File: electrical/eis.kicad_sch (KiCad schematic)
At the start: 51 parts

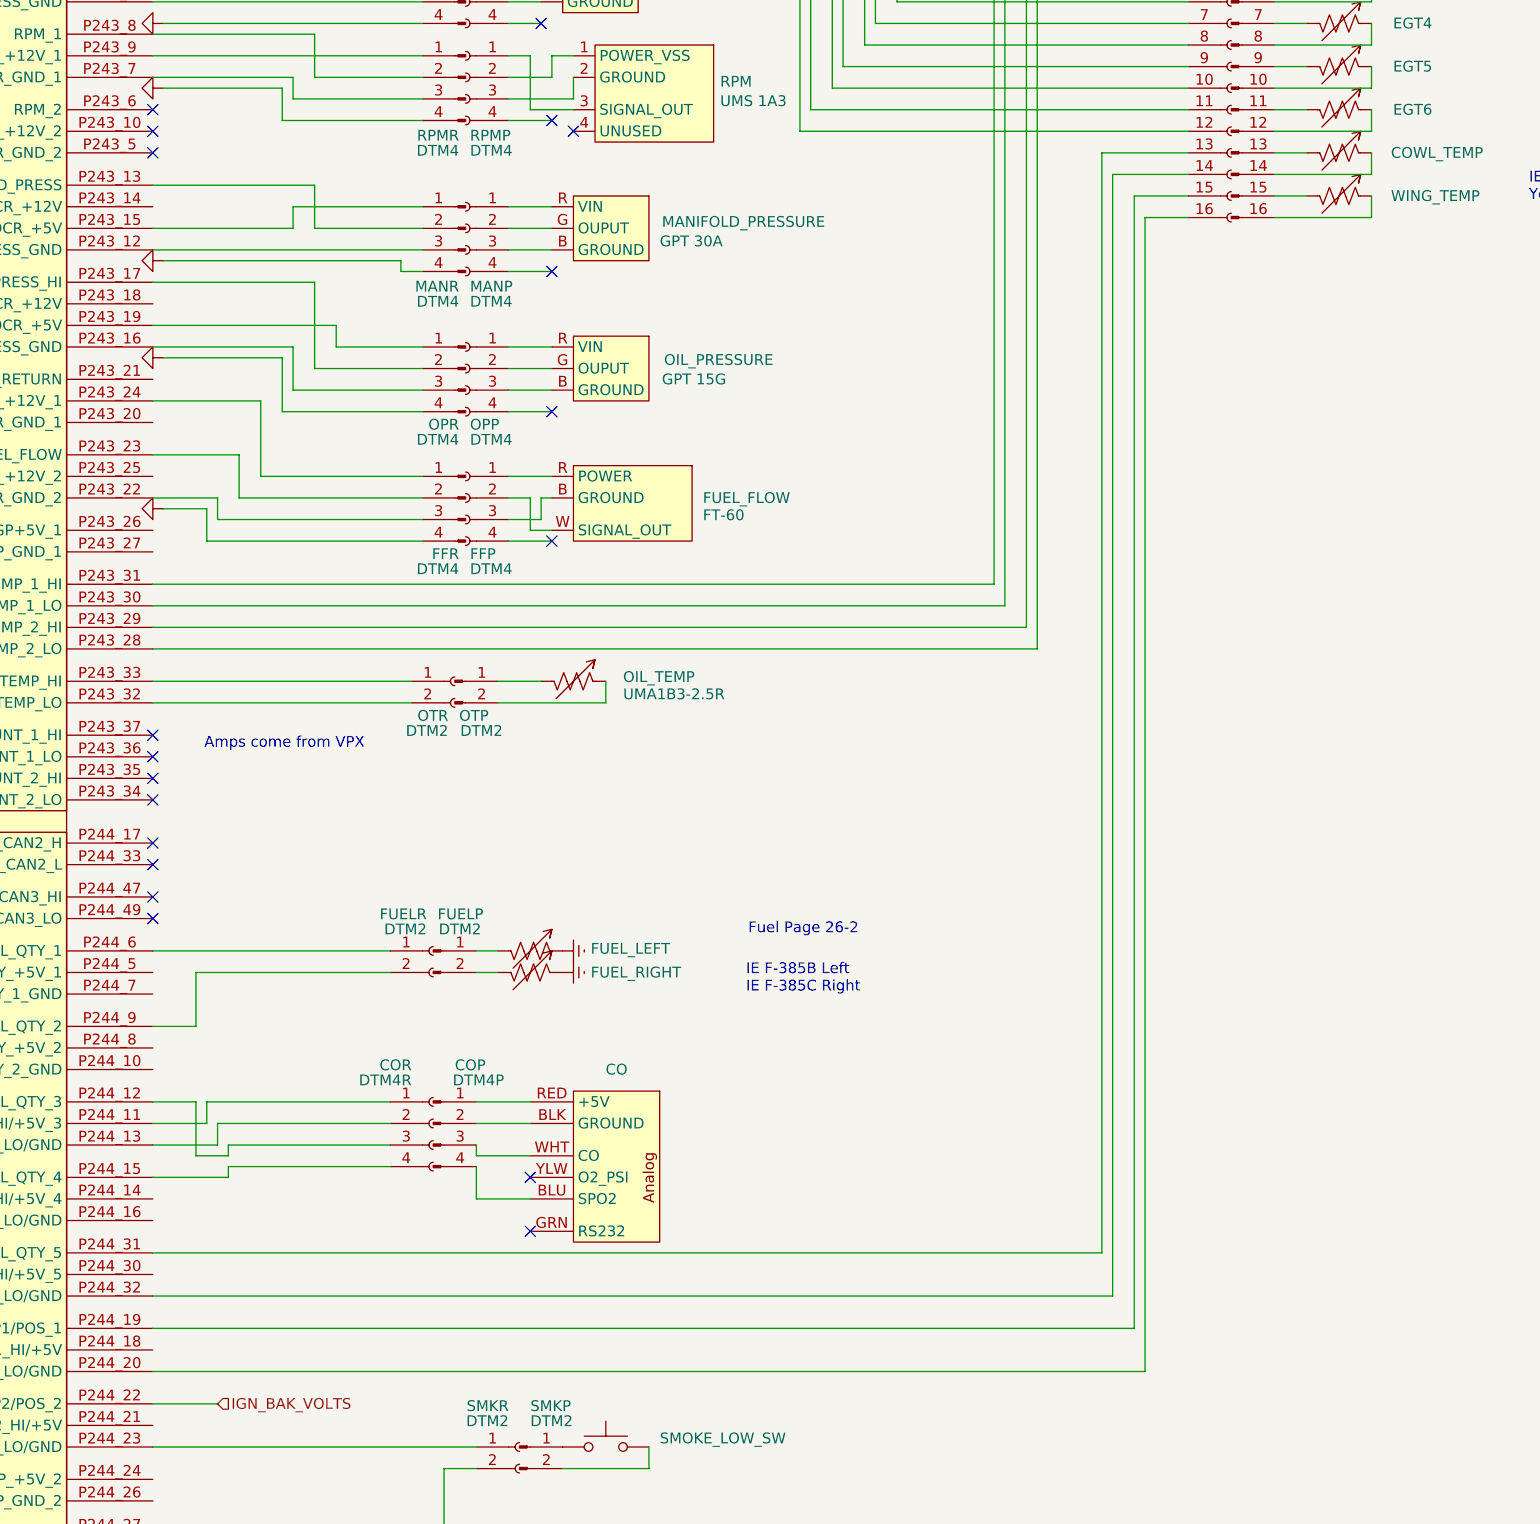
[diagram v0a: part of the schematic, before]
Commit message: Removed air temps from GP inputs as not compatible
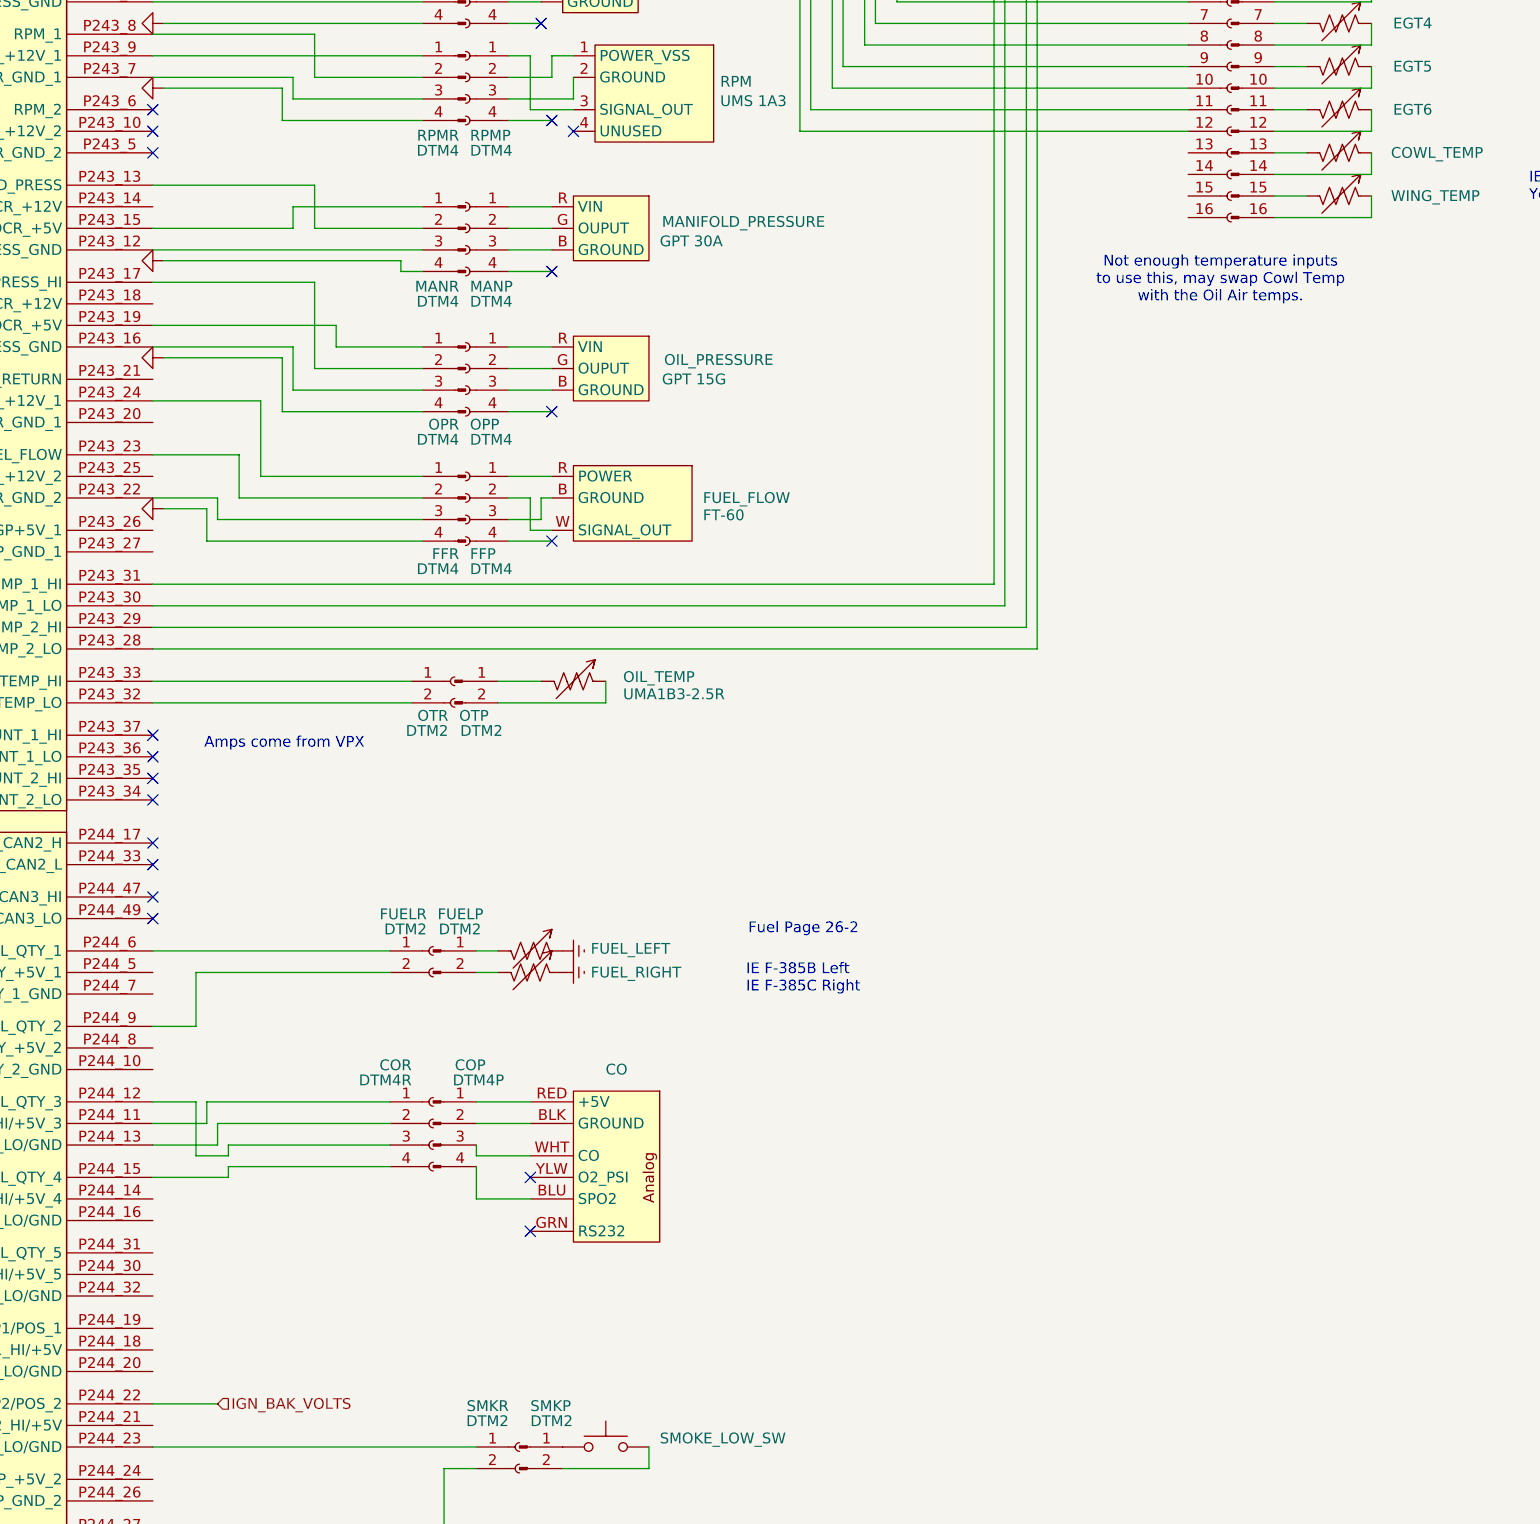
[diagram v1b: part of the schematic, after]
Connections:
- net at EGTS.13 (Pin_13): no longer GEA24.P244_31 (POS_5/GP_5/FUEL_QTY_5)
- net at EGTS.14 (Pin_14): no longer GEA24.P244_32 (POS_5_LO/GND)
- net at EGTS.15 (Pin_15): no longer GEA24.P244_19 (GP1/POS_1)
- net at EGTS.16 (Pin_16): no longer GEA24.P244_20 (GP1_LO/GND)
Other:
- note added: "Not enough temperature inputs to use this, may swap Cowl Temp with the Oil Air temps."
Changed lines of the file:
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@@
 	(title_block
 		(title "EIS")
-		(date "2025-10-22")
-		(rev "1.1.18")
+		(date "2025-10-23")
+		(rev "1.1.19")
 		(company "N78HR")
 	)
@@
 		)
 	)
+	(text "Not enough temperature inputs\nto use this, may swap Cowl Temp\nwith the Oil Air temps."
+		(exclude_from_sim no)
+		(at 193.04 152.146 0)
+		(effects
+			(font
+				(size 1.27 1.27)
+			)
+		)
+	)
 	(text "IE Probes\nYellow/Red (yellow +)"
 		(exclude_from_sim no)
@@
 	(wire
 		(pts
-			(xy 67.31 280.67) (xy 184.15 280.67)
-		)
-		(stroke
-			(width 0)
-			(type default)
-		)
-	)
-	(wire
-		(pts
 			(xy 116.84 132.08) (xy 111.76 132.08)
 		)
@@
 	(wire
 		(pts
-			(xy 182.88 275.59) (xy 182.88 142.24)
-		)
-		(stroke
-			(width 0)
-			(type default)
-		)
-	)
-	(wire
-		(pts
-			(xy 67.31 275.59) (xy 182.88 275.59)
-		)
-		(stroke
-			(width 0)
-			(type default)
-		)
-	)
-	(wire
-		(pts
 			(xy 74.93 251.46) (xy 95.25 251.46)
 		)
@@
 	(wire
 		(pts
-			(xy 180.34 139.7) (xy 180.34 271.78)
-		)
-		(stroke
-			(width 0)
-			(type default)
-		)
-	)
-	(wire
-		(pts
 			(xy 67.31 104.14) (xy 144.78 104.14)
 		)
@@
 	(wire
 		(pts
-			(xy 182.88 142.24) (xy 189.23 142.24)
-		)
-		(stroke
-			(width 0)
-			(type default)
-		)
-	)
-	(wire
-		(pts
 			(xy 67.31 187.96) (xy 166.37 187.96)
 		)
@@
 	(wire
 		(pts
-			(xy 67.31 266.7) (xy 179.07 266.7)
-		)
-		(stroke
-			(width 0)
-			(type default)
-		)
-	)
-	(wire
-		(pts
 			(xy 67.31 125.73) (xy 99.06 125.73)
 		)
@@
 	(wire
 		(pts
-			(xy 67.31 271.78) (xy 180.34 271.78)
-		)
-		(stroke
-			(width 0)
-			(type default)
-		)
-	)
-	(wire
-		(pts
 			(xy 67.31 99.06) (xy 148.59 99.06)
 		)
@@
 	(wire
 		(pts
-			(xy 179.07 137.16) (xy 189.23 137.16)
-		)
-		(stroke
-			(width 0)
-			(type default)
-		)
-	)
-	(wire
-		(pts
 			(xy 67.31 257.81) (xy 76.2 257.81)
 		)
@@
 	(wire
 		(pts
-			(xy 184.15 280.67) (xy 184.15 144.78)
-		)
-		(stroke
-			(width 0)
-			(type default)
-		)
-	)
-	(wire
-		(pts
 			(xy 109.22 128.27) (xy 114.3 128.27)
 		)
@@
 	(wire
 		(pts
-			(xy 184.15 144.78) (xy 189.23 144.78)
-		)
-		(stroke
-			(width 0)
-			(type default)
-		)
-	)
-	(wire
-		(pts
 			(xy 111.76 132.08) (xy 111.76 125.73)
 		)
@@
 		)
 	)
-	(wire
-		(pts
-			(xy 180.34 139.7) (xy 189.23 139.7)
-		)
-		(stroke
-			(width 0)
-			(type default)
-		)
-	)
-	(wire
-		(pts
-			(xy 179.07 137.16) (xy 179.07 266.7)
-		)
-		(stroke
-			(width 0)
-			(type default)
-		)
-	)

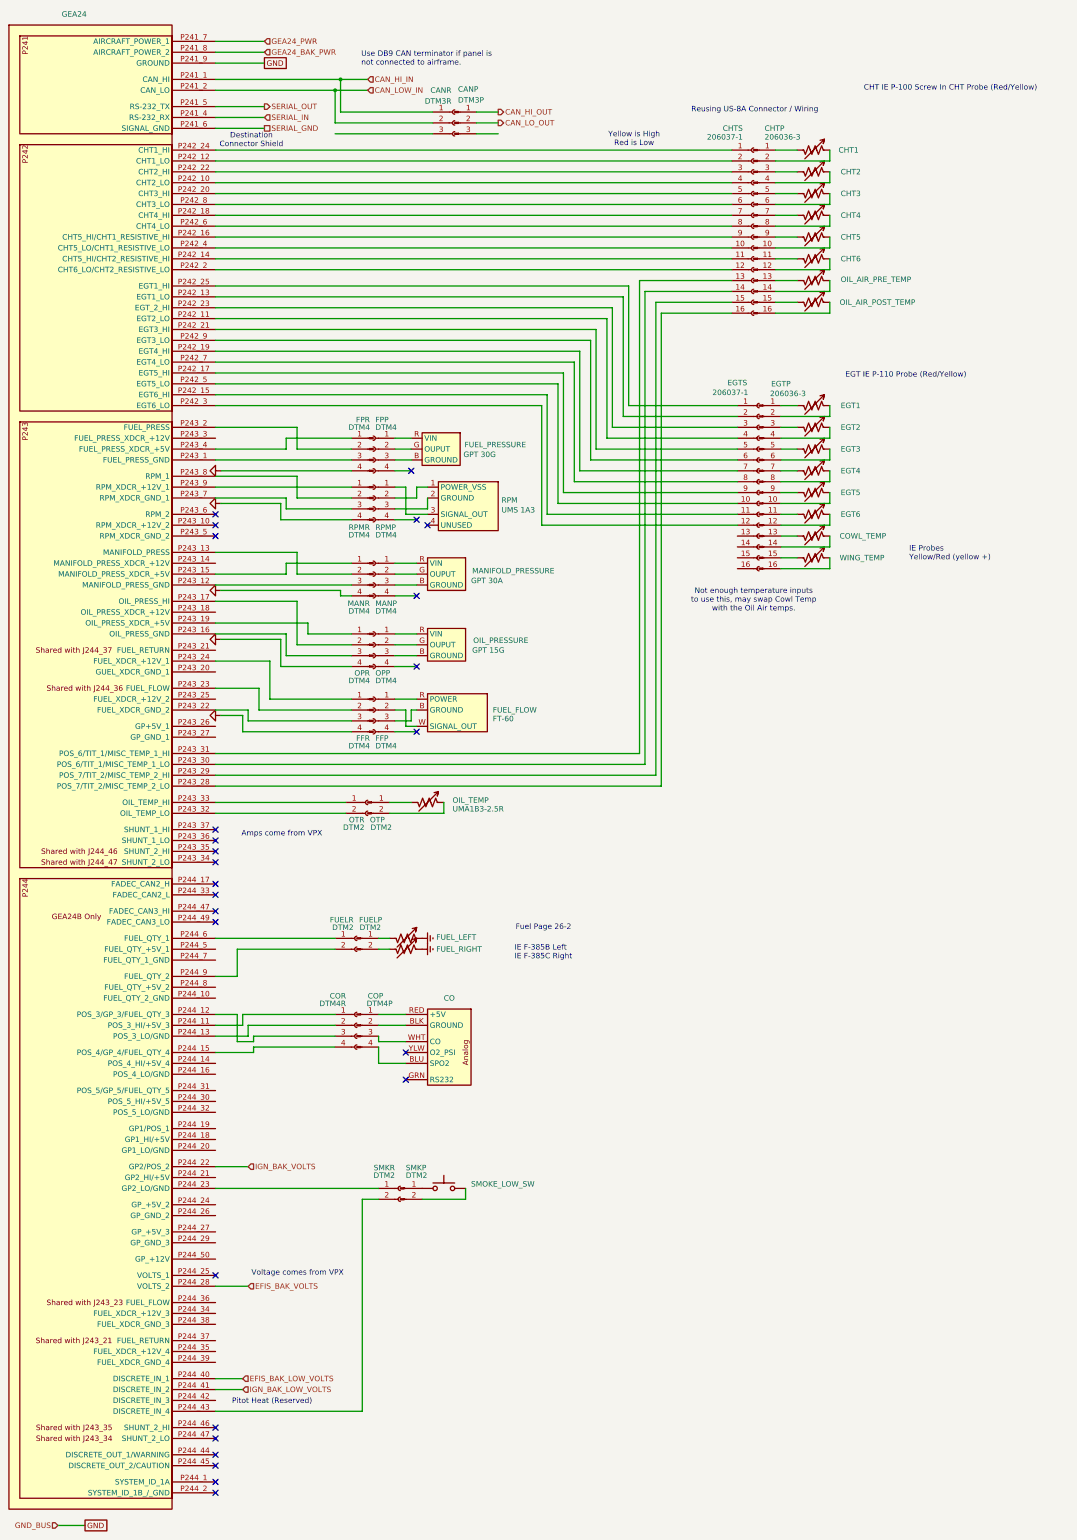
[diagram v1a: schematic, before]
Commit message: Corrected all rececptacle/plug polarity and naming.
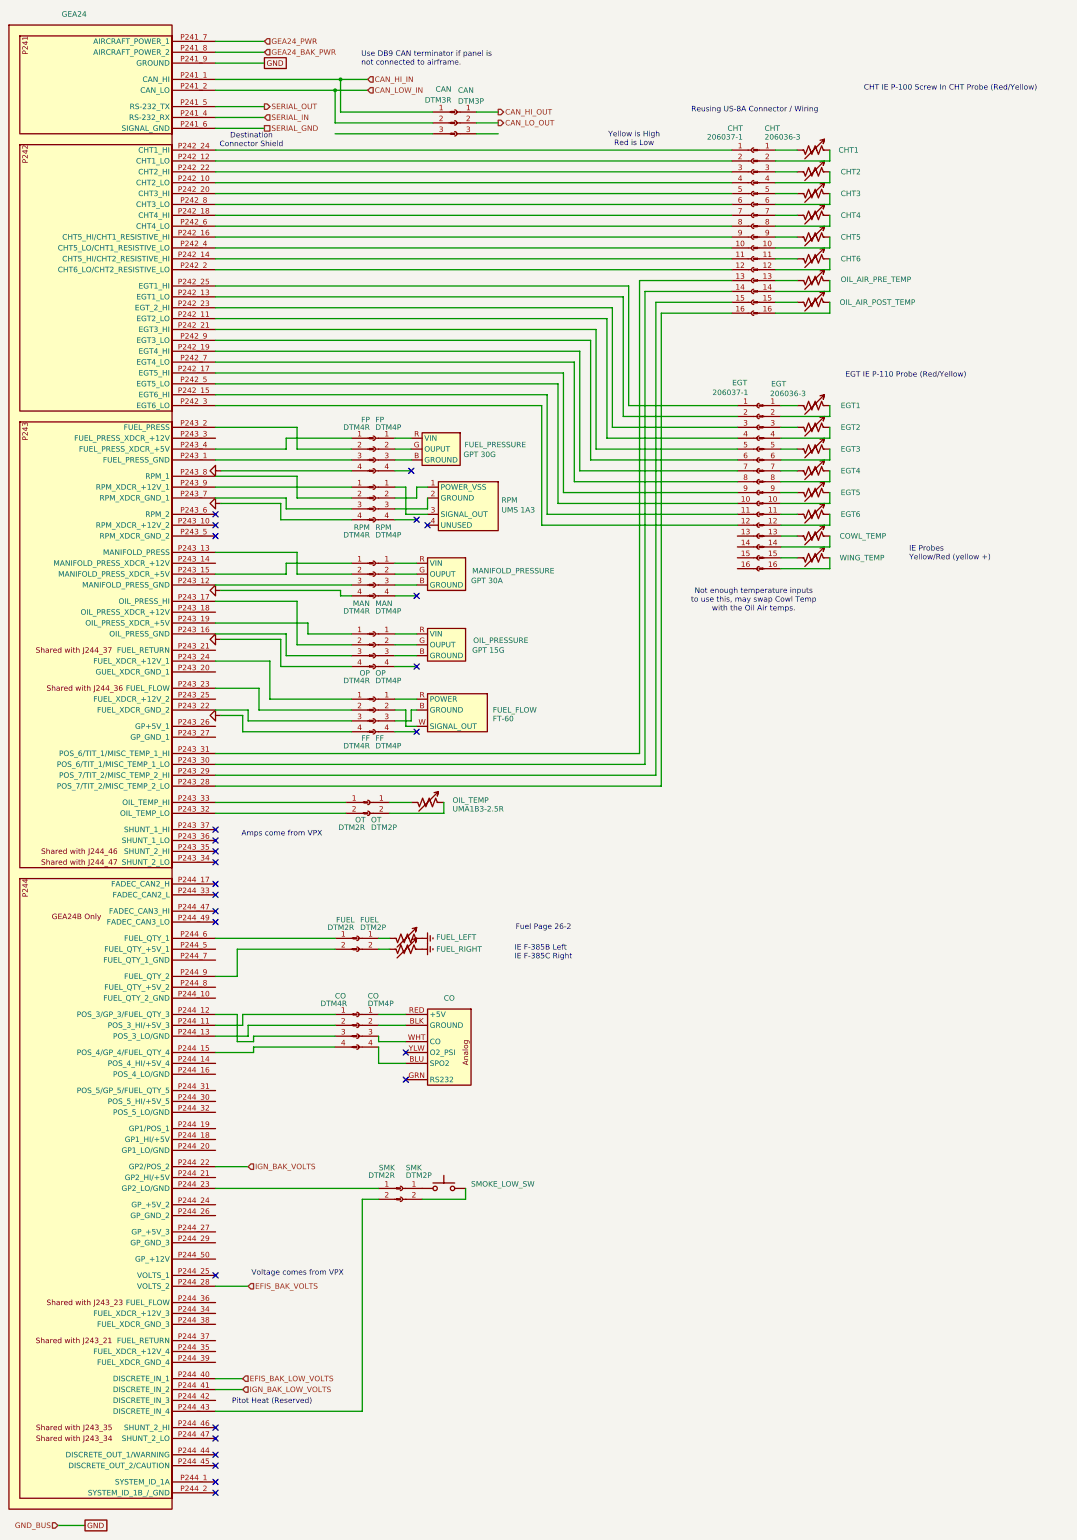
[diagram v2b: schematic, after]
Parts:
- CAN: renamed from CANP; value DTM3P -> DTM3R
- CAN: renamed from CANR; value DTM3R -> DTM3P
- CO: renamed from COP; value DTM4P -> DTM4R
- CO: renamed from COR; value DTM4R -> DTM4P
- FF: renamed from FFR; value DTM4 -> DTM4R
- FF: renamed from FFP; value DTM4 -> DTM4P
- FP: renamed from FPP; value DTM4 -> DTM4P
- FP: renamed from FPR; value DTM4 -> DTM4R
- FUEL: renamed from FUELR; value DTM2 -> DTM2P
- FUEL: renamed from FUELP; value DTM2 -> DTM2R
- MAN: renamed from MANR; value DTM4 -> DTM4R
- MAN: renamed from MANP; value DTM4 -> DTM4P
- OP: renamed from OPR; value DTM4 -> DTM4R
- OP: renamed from OPP; value DTM4 -> DTM4P
- OT: renamed from OTR; value DTM2 -> DTM2P
- OT: renamed from OTP; value DTM2 -> DTM2R
- RPM: renamed from RPMP; value DTM4 -> DTM4P
- RPM: renamed from RPMR; value DTM4 -> DTM4R
- SMK: renamed from SMKR; value DTM2 -> DTM2P
- SMK: renamed from SMKP; value DTM2 -> DTM2R
- renumbered CHTS to CHT, CHTP to CHT, EGTS to EGT, EGTP to EGT
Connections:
- net CAN_HI_IN: now also CAN.1 (Pin_1); no longer CAN.1 (Pin_1)
- net CAN_HI_OUT: now also CAN.1 (Pin_1); no longer CAN.1 (Pin_1)
- net CAN_LOW_IN: now also CAN.2 (Pin_2); no longer CAN.2 (Pin_2)
- net CAN_LO_OUT: now also CAN.2 (Pin_2); no longer CAN.2 (Pin_2)
- net at FUEL.1 (Pin_1): now also FUEL_LEFT.2; no longer GEA24.P244_6 (FUEL_QTY_1)
- net at FUEL.2 (Pin_2): now also FUEL_RIGHT.2; no longer GEA24.P244_9 (FUEL_QTY_2)
- net at SMK.1 (Pin_1): now also SMOKE_LOW_SW.1; no longer GEA24.P244_23 (GP2_LO/GND)
- net at SMK.2 (Pin_2): now also SMOKE_LOW_SW.2; no longer GEA24.P244_43 (DISCRETE_IN_4)
- net at CO.1 (Pin_1): now also GEA24.P244_11 (POS_3_HI/+5V_3); no longer CO.RED (+5V)
- net at CO.2 (Pin_2): now also GEA24.P244_13 (POS_3_LO/GND); no longer CO.BLK (GROUND)
- net at CO.3 (Pin_3): now also GEA24.P244_12 (POS_3/GP_3/FUEL_QTY_3); no longer CO.WHT (CO)
- net at CO.4 (Pin_4): now also GEA24.P244_15 (POS_4/GP_4/FUEL_QTY_4); no longer CO.BLU (SPO2)
- net at GEA24.P243_32 (OIL_TEMP_LO): now also OT.2 (Pin_2); no longer OT.2 (Pin_2)
- net at GEA24.P243_33 (OIL_TEMP_HI): now also OT.1 (Pin_1); no longer OT.1 (Pin_1)
- net at CO.1 (Pin_1): now also CO.RED (+5V); no longer GEA24.P244_11 (POS_3_HI/+5V_3)
- net at CO.3 (Pin_3): now also CO.WHT (CO); no longer GEA24.P244_12 (POS_3/GP_3/FUEL_QTY_3)
- net at CO.2 (Pin_2): now also CO.BLK (GROUND); no longer GEA24.P244_13 (POS_3_LO/GND)
- net at CO.4 (Pin_4): now also CO.BLU (SPO2); no longer GEA24.P244_15 (POS_4/GP_4/FUEL_QTY_4)
- net at FUEL.1 (Pin_1): now also GEA24.P244_6 (FUEL_QTY_1); no longer FUEL_LEFT.2
- net at FUEL.2 (Pin_2): now also GEA24.P244_9 (FUEL_QTY_2); no longer FUEL_RIGHT.2
- net at SMK.1 (Pin_1): now also GEA24.P244_23 (GP2_LO/GND); no longer SMOKE_LOW_SW.1
- net at SMK.2 (Pin_2): now also GEA24.P244_43 (DISCRETE_IN_4); no longer SMOKE_LOW_SW.2
- net at OIL_TEMP.1: now also OT.2 (Pin_2); no longer OT.2 (Pin_2)
- net at OIL_TEMP.2: now also OT.1 (Pin_1); no longer OT.1 (Pin_1)
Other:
- moved on the sheet: CAN, CO, FUEL, OT, SMK
